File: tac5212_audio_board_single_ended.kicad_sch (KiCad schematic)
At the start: 94 parts, among them J1002 TAC5212, U1 Single Buffer - 74LVC1G125GV,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, U2 3.3v LDO - TLV74133PDBVR

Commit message: UPDATE
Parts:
- added G108: jumper, project_fp:jumper_slice, symbol proejct_lib:Jumper_2_Bridged
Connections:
- net Earth: now also E1.1 (A), E2.1 (A), G108.2 (B); no longer E1.2 (B), E2.2 (B)
- net GNDD: no longer T*C1.2, T*C2.2, T*C3.2, U2.2 (GND)
- net at board_outline1.49 (AGND): now also E1.2 (B); no longer E1.1 (A)
- net at board_outline1.50 (AGND): now also E2.2 (B); no longer E2.1 (A)
- new net: G108.1 (A), T*C1.2, T*C2.2, T*C3.2, U2.2 (GND)
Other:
- moved on the sheet: E1, E2
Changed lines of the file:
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@@
 	(wire
 		(pts
+			(xy 110.49 372.11) (xy 104.14 372.11)
+		)
+		(stroke
+			(width 0)
+			(type default)
+		)
+	)
+	(wire
+		(pts
 			(xy 218.44 168.91) (xy 222.25 168.91)
 		)
@@
 	(wire
 		(pts
-			(xy 90.17 367.03) (xy 90.17 365.76)
-		)
-		(stroke
-			(width 0)
-			(type default)
-		)
-	)
-	(wire
-		(pts
 			(xy 190.5 91.44) (xy 199.39 91.44)
 		)
@@
 	(wire
 		(pts
+			(xy 90.17 372.11) (xy 93.98 372.11)
+		)
+		(stroke
+			(width 0)
+			(type default)
+		)
+	)
+	(wire
+		(pts
 			(xy 49.53 294.64) (xy 66.04 294.64)
 		)
@@
 	(wire
 		(pts
+			(xy 90.17 372.11) (xy 90.17 365.76)
+		)
+		(stroke
+			(width 0)
+			(type default)
+		)
+	)
+	(wire
+		(pts
 			(xy 71.12 156.21) (xy 71.12 157.48)
 		)
@@
 	)
 	(symbol
+		(lib_id "proejct_lib:Earth")
+		(at 110.49 372.11 0)
+		(mirror y)
+		(unit 1)
+		(exclude_from_sim no)
+		(in_bom yes)
+		(on_board yes)
+		(dnp no)
+		(fields_autoplaced yes)
+		(property "Reference" "#PWR0108"
+			(at 110.49 378.46 0)
+			(effects
+				(font
+					(size 1 1)
+				)
+				(hide yes)
+			)
+		)
+		(property "Value" "Earth"
+			(at 110.49 375.92 0)
+			(effects
+				(font
+					(size 0.8 0.8)
+				)
+				(hide yes)
+			)
+		)
+		(property "Footprint" ""
+			(at 110.49 372.11 0)
+			(effects
+				(font
+					(size 0.8 0.8)
+				)
+				(hide yes)
+			)
+		)
+		(property "Datasheet" "~"
+			(at 110.49 372.11 0)
+			(effects
+				(font
+					(size 0.8 0.8)
+				)
+				(hide yes)
+			)
+		)
+		(property "Description" ""
+			(at 110.49 372.11 0)
+			(effects
+				(font
+					(size 1.27 1.27)
+				)
+				(hide yes)
+			)
+		)
+		(pin "1"
+		)
+		(instances
+			(project "tac5212_audio_board_single_ended"
+				(path "/8cee3af6-3893-45a9-89a4-21657973eeff"
+					(reference "#PWR0108")
+					(unit 1)
+				)
+			)
+		)
+	)
+	(symbol
 		(lib_name "Jumper_NO_Small-Device_1")
 		(lib_id "proejct_lib:Jumper_NO_Small-Device_1")
@@
 	(symbol
 		(lib_id "proejct_lib:Jumper_2_Bridged")
-		(at 125.73 287.02 0)
+		(at 125.73 287.02 180)
 		(unit 1)
 		(exclude_from_sim yes)
@@
 		(dnp yes)
 		(property "Reference" "E2"
-			(at 131.064 283.464 0)
+			(at 120.396 290.576 0)
 			(effects
 				(font
@@
 		)
 		(property "Value" "jumper"
-			(at 119.38 283.21 0)
+			(at 132.08 290.83 0)
 			(effects
 				(font
@@
 	)
 	(symbol
-		(lib_id "proejct_lib:GNDD")
-		(at 90.17 367.03 0)
-		(unit 1)
-		(exclude_from_sim no)
-		(in_bom yes)
-		(on_board yes)
-		(dnp no)
-		(fields_autoplaced yes)
-		(property "Reference" "#PWR013"
-			(at 90.17 373.38 0)
-			(effects
-				(font
-					(size 1 1)
-				)
-				(hide yes)
-			)
-		)
-		(property "Value" "GNDD"
-			(at 90.17 371.094 0)
-			(effects
-				(font
-					(size 0.8 0.8)
-				)
-			)
-		)
-		(property "Footprint" ""
-			(at 90.17 367.03 0)
-			(effects
-				(font
-					(size 0.8 0.8)
-				)
-				(hide yes)
-			)
-		)
-		(property "Datasheet" ""
-			(at 90.17 367.03 0)
-			(effects
-				(font
-					(size 0.8 0.8)
-				)
-				(hide yes)
-			)
-		)
-		(property "Description" ""
-			(at 90.17 367.03 0)
-			(effects
-				(font
-					(size 1.27 1.27)
-				)
-				(hide yes)
-			)
-		)
-		(pin "1"
-		)
-		(instances
-			(project "tac5212_audio_board_single_ended"
-				(path "/8cee3af6-3893-45a9-89a4-21657973eeff"
-					(reference "#PWR013")
-					(unit 1)
-				)
-			)
-		)
-	)
-	(symbol
 		(lib_id "proejct_lib:Jumper_NO_Small-Device")
 		(at 241.3 118.11 0)
@@
 	)
 	(symbol
+		(lib_id "proejct_lib:Jumper_2_Bridged")
+		(at 99.06 372.11 0)
+		(unit 1)
+		(exclude_from_sim yes)
+		(in_bom yes)
+		(on_board yes)
+		(dnp yes)
+		(property "Reference" "G108"
+			(at 104.394 371.094 0)
+			(effects
+				(font
+					(size 1.27 1.27)
+				)
+			)
+		)
+		(property "Value" "jumper"
+			(at 92.71 370.84 0)
+			(effects
+				(font
+					(size 1.27 1.27)
+				)
+				(hide yes)
+			)
+		)
+		(property "Footprint" "project_fp:jumper_slice"
+			(at 99.06 372.11 0)
+			(effects
+				(font
+					(size 1.27 1.27)
+				)
+				(hide yes)
+			)
+		)
+		(property "Datasheet" "~"
+			(at 99.06 372.11 0)
+			(effects
+				(font
+					(size 1.27 1.27)
+				)
+				(hide yes)
+			)
+		)
+		(property "Description" "Jumper, open"
+			(at 99.06 372.11 0)
+			(effects
+				(font
+					(size 1.27 1.27)
+				)
+				(hide yes)
+			)
+		)
+		(property "Label" "G"
+			(at 99.06 372.11 0)
+			(effects
+				(font
+					(size 1.27 1.27)
+				)
+				(hide yes)
+			)
+		)
+		(property "Package / Case" "DNP"
+			(at 99.06 372.11 0)
+			(effects
+				(font
+					(size 1.27 1.27)
+				)
+				(hide yes)
+			)
+		)
+		(property "TAC5212EVM" "n/a"
+			(at 99.06 372.11 0)
+			(effects
+				(font
+					(size 1.27 1.27)
+				)
+				(hide yes)
+			)
+		)
+		(pin "1"
+		)
+		(pin "2"
+		)
+		(instances
+			(project "tac5212_audio_board_single_ended"
+				(path "/8cee3af6-3893-45a9-89a4-21657973eeff"
+					(reference "G108")
+					(unit 1)
+				)
+			)
+		)
+	)
+	(symbol
 		(lib_id "proejct_lib:GNDD")
 		(at 144.78 162.56 0)
@@
 	(symbol
 		(lib_id "proejct_lib:Jumper_2_Bridged")
-		(at 125.73 281.94 0)
+		(at 125.73 281.94 180)
 		(unit 1)
 		(exclude_from_sim yes)
@@
 		(dnp yes)
 		(property "Reference" "E1"
-			(at 131.064 280.924 0)
+			(at 120.396 282.956 0)
 			(effects
 				(font
@@
 		)
 		(property "Value" "jumper"
-			(at 119.38 280.67 0)
+			(at 132.08 283.21 0)
 			(effects
 				(font

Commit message: update
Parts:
- board_outline1: now not fitted
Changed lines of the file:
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@@
 		(in_bom yes)
 		(on_board yes)
-		(dnp no)
+		(dnp yes)
 		(property "Reference" "board_outline1"
 			(at 91.44 217.17 0)

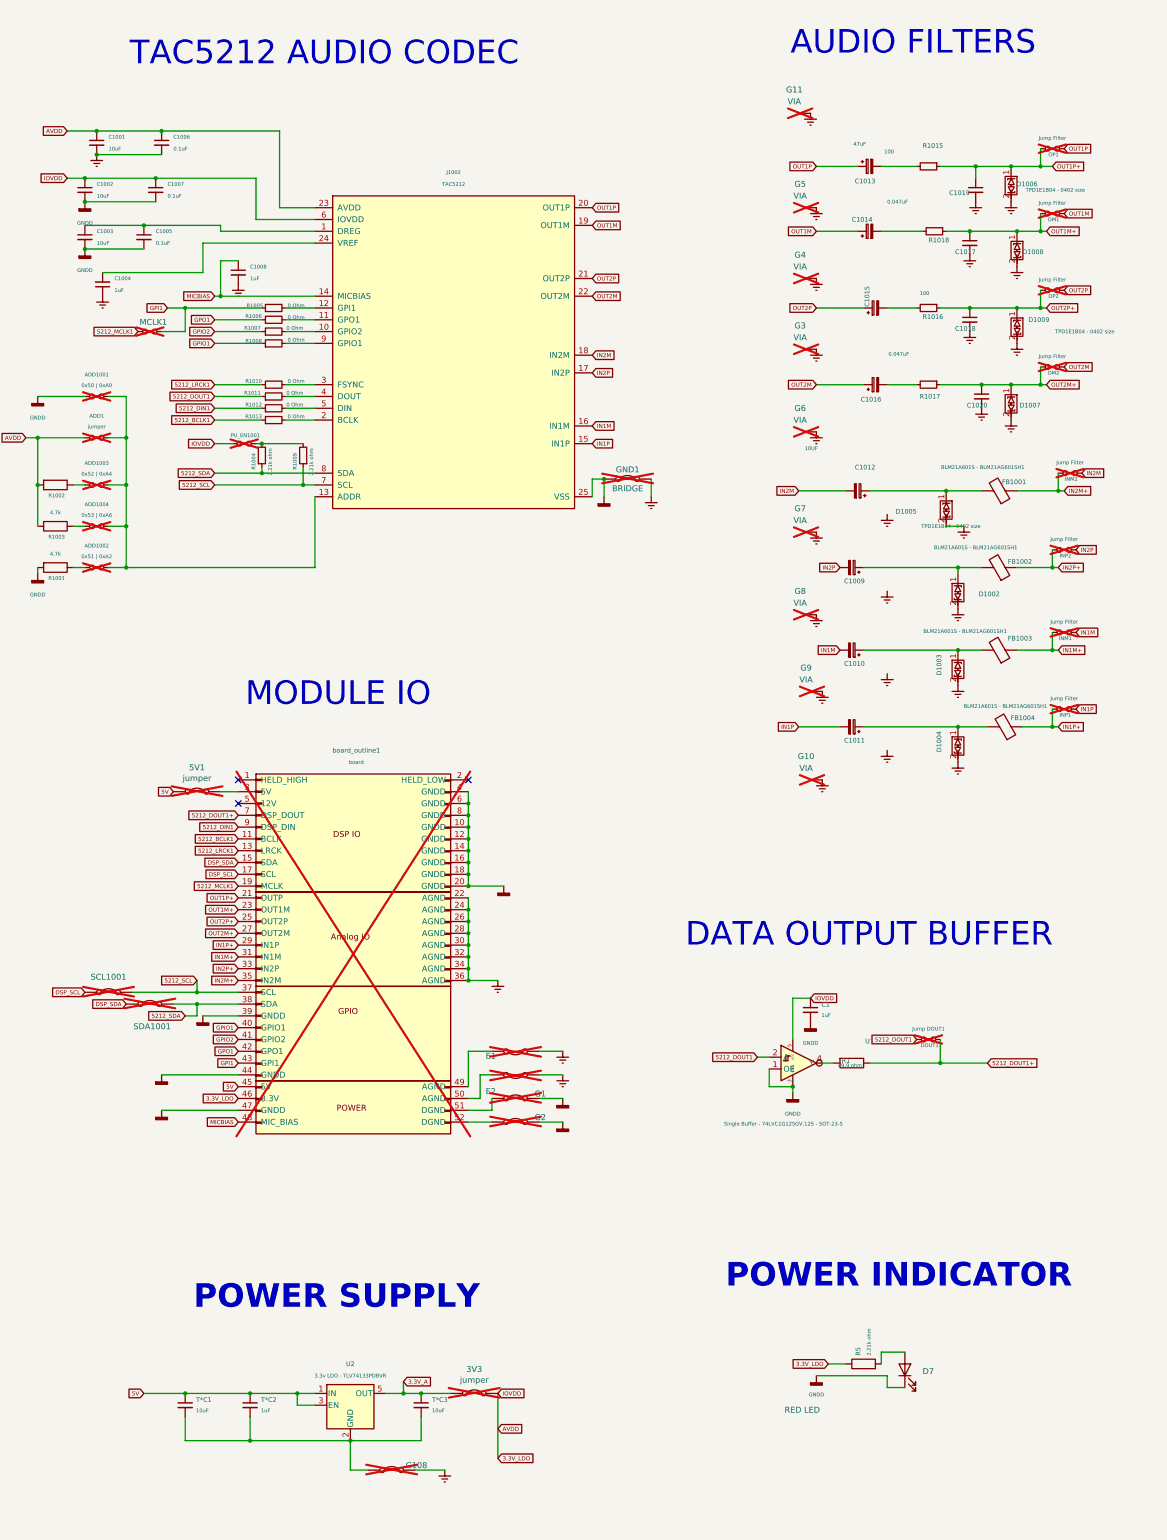
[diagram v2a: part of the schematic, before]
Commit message: added enable (held-high)
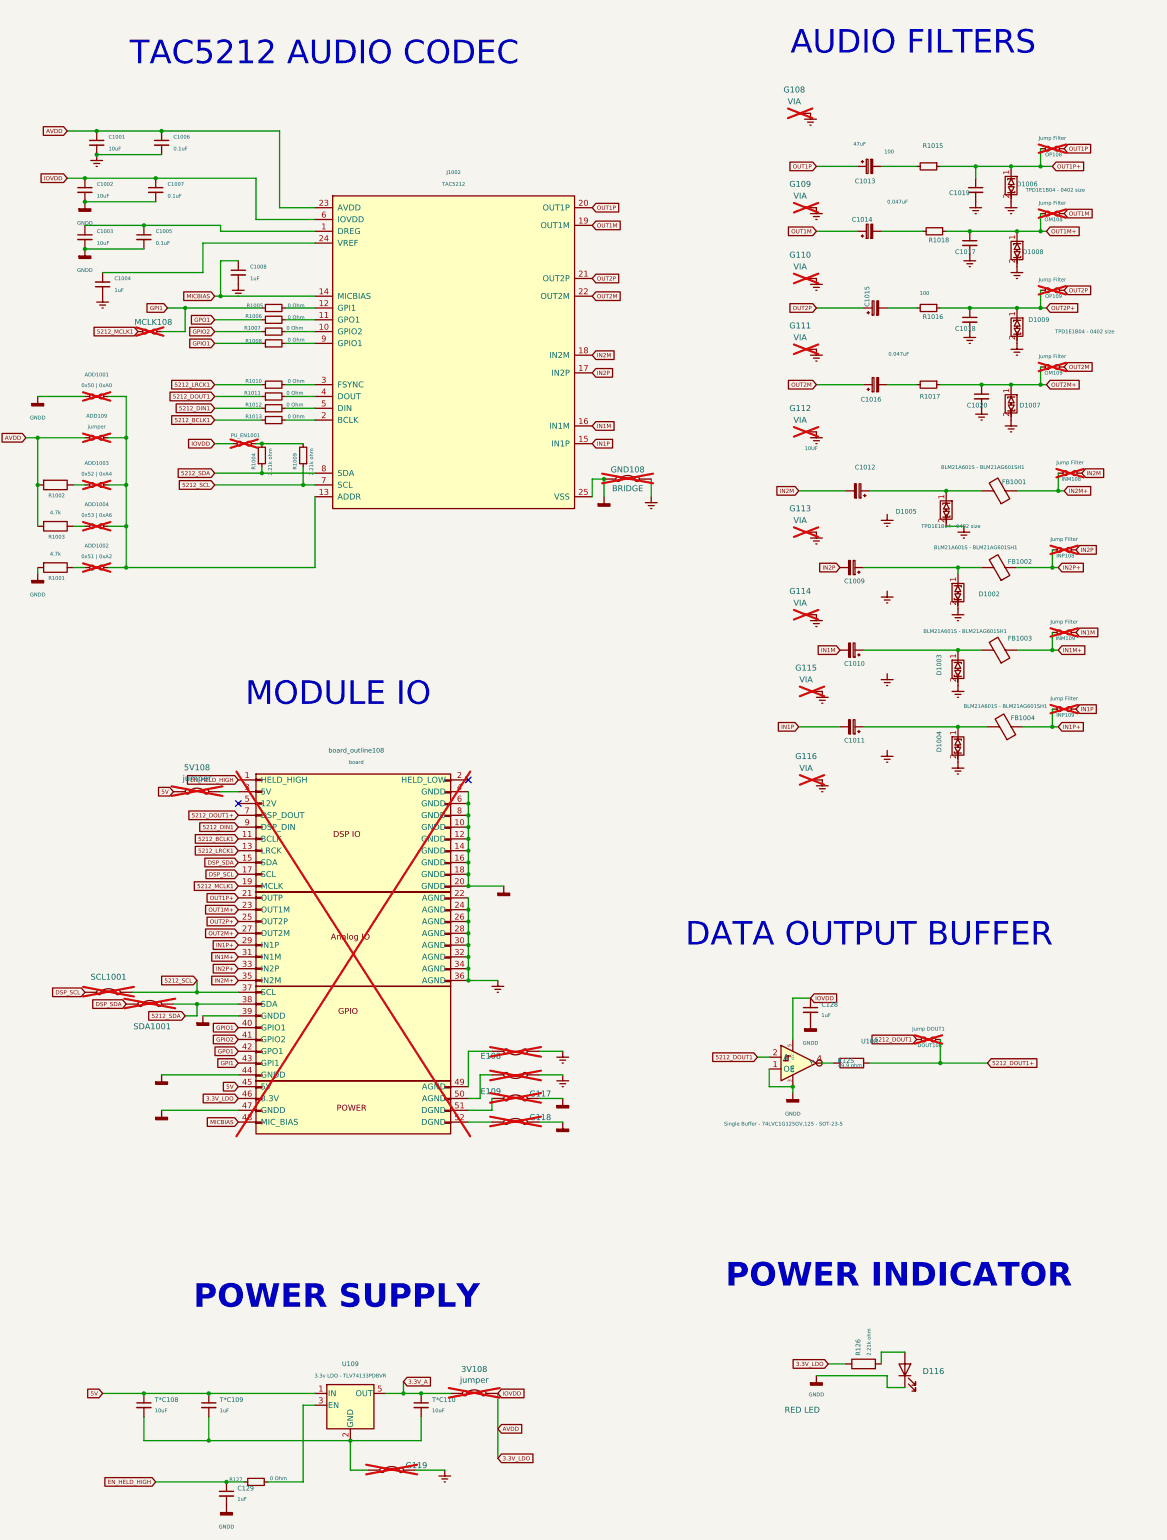
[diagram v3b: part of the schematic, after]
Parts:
- added C129: 1uF, Capacitor_SMD:C_0603_1608Metric_Pad1.08x0.95mm_HandSolder, symbol proejct_lib:C_Small
- added R127: 0 Ohm, Resistor_SMD:R_0402_1005Metric_Pad0.72x0.64mm_HandSolder, symbol proejct_lib:R_Small
- renumbered 3V3 to 3V108, 5V1 to 5V108, ADD1 to ADD109, C1 to C128, D7 to D116, DOUT1 to DOUT108, E1 to E108, E2 to E109, G11 to G108, G5 to G109, G4 to G110, G3 to G111, G6 to G112, G7 to G113, G8 to G114, G9 to G115, G10 to G116, G1 to G117, G2 to G118, G108 to G119, GND1 to GND108, INM2 to INM108, INM1 to INM109, INP2 to INP108, INP1 to INP109, MCLK1 to MCLK108, OM1 to OM108, OM2 to OM109, OP1 to OP108, OP2 to OP109, R1 to R125, R5 to R126, T*C1 to T*C108, T*C2 to T*C109, T*C3 to T*C110, U1 to U108, U2 to U109, board_outline1 to board_outline108
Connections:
- net 5V: no longer U109.3 (EN)
- net GNDD: now also C129.2
- net EN_HELD_HIGH: now reaches board_outline108.1 (HELD_HIGH)
- net EN_HELD_HIGH: now also C129.1, R127.1
- new net: R127.2, U109.3 (EN)
- no-connect marks 3 -> 2
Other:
- moved on the sheet: T*C108, T*C109

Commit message: update
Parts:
- R1004, R1009: TAC5212EVM RC0402FR-07100KL -> RC0402FR-072K21L
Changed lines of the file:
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@@
 			)
 		)
-		(property "TAC5212EVM" "RC0402FR-07100KL"
+		(property "TAC5212EVM" "RC0402FR-072K21L"
 			(at 71.12 153.67 0)
 			(effects
@@
 			)
 		)
-		(property "TAC5212EVM" "RC0402FR-07100KL"
+		(property "TAC5212EVM" "RC0402FR-072K21L"
 			(at 80.01 153.67 0)
 			(effects

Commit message: update
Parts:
- removed ADD109: jumper, project_fp:SolderJumper-2_Open_Pad0.5x1.0mm_ADDR, symbol proejct_lib:Jumper_NO_Small-Device
- J1002: footprint project_fp:TAC5212IRGER-24-1EP_4x4mm -> project_fp:VQFN-24-1EP_4x4mm_P0.5mm_EP2.45x2.45mm_ThermalVias
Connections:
- net GNDD: now also J1002.A1 (VSS), J1002.A2 (VSS), J1002.A3 (VSS), J1002.A4 (VSS)
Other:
- moved on the sheet: ADD1001, ADD1003, ADD1004, GND108, R1002, R1003

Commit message: update
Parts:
- renumbered INM109 to INM1, INM108 to INM2, INP109 to INP1, INP108 to INP2, OM108 to OM1, OM109 to OM2, OP108 to OP1, OP109 to OP2
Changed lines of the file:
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@@
 		(on_board yes)
 		(dnp yes)
-		(property "Reference" "INM109"
+		(property "Reference" "INM1"
 			(at 244.094 193.04 0)
 			(effects
@@
 			(project "tac5212_audio_board_single_ended"
 				(path "/8cee3af6-3893-45a9-89a4-21657973eeff"
-					(reference "INM109")
+					(reference "INM1")
 					(unit 1)
 				)
@@
 		(on_board yes)
 		(dnp yes)
-		(property "Reference" "OP108"
+		(property "Reference" "OP1"
 			(at 241.554 88.9 0)
 			(effects
@@
 			(project "tac5212_audio_board_single_ended"
 				(path "/8cee3af6-3893-45a9-89a4-21657973eeff"
-					(reference "OP108")
+					(reference "OP1")
 					(unit 1)
 				)
@@
 		(on_board yes)
 		(dnp yes)
-		(property "Reference" "OM109"
+		(property "Reference" "OM2"
 			(at 241.554 135.89 0)
 			(effects
@@
 			(project "tac5212_audio_board_single_ended"
 				(path "/8cee3af6-3893-45a9-89a4-21657973eeff"
-					(reference "OM109")
+					(reference "OM2")
 					(unit 1)
 				)
@@
 		(on_board yes)
 		(dnp yes)
-		(property "Reference" "OM108"
+		(property "Reference" "OM1"
 			(at 241.554 102.87 0)
 			(effects
@@
 			(project "tac5212_audio_board_single_ended"
 				(path "/8cee3af6-3893-45a9-89a4-21657973eeff"
-					(reference "OM108")
+					(reference "OM1")
 					(unit 1)
 				)
@@
 		(on_board yes)
 		(dnp yes)
-		(property "Reference" "INP109"
+		(property "Reference" "INP1"
 			(at 244.094 209.55 0)
 			(effects
@@
 			(project "tac5212_audio_board_single_ended"
 				(path "/8cee3af6-3893-45a9-89a4-21657973eeff"
-					(reference "INP109")
+					(reference "INP1")
 					(unit 1)
 				)
@@
 		(on_board yes)
 		(dnp yes)
-		(property "Reference" "INM108"
+		(property "Reference" "INM2"
 			(at 245.364 158.75 0)
 			(effects
@@
 			(project "tac5212_audio_board_single_ended"
 				(path "/8cee3af6-3893-45a9-89a4-21657973eeff"
-					(reference "INM108")
+					(reference "INM2")
 					(unit 1)
 				)
@@
 		(on_board yes)
 		(dnp yes)
-		(property "Reference" "INP108"
+		(property "Reference" "INP2"
 			(at 244.094 175.26 0)
 			(effects
@@
 			(project "tac5212_audio_board_single_ended"
 				(path "/8cee3af6-3893-45a9-89a4-21657973eeff"
-					(reference "INP108")
+					(reference "INP2")
 					(unit 1)
 				)
@@
 		(on_board yes)
 		(dnp yes)
-		(property "Reference" "OP109"
+		(property "Reference" "OP2"
 			(at 241.554 119.38 0)
 			(effects
@@
 			(project "tac5212_audio_board_single_ended"
 				(path "/8cee3af6-3893-45a9-89a4-21657973eeff"
-					(reference "OP109")
+					(reference "OP2")
 					(unit 1)
 				)

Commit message: update
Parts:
- added TAC108-Q1: TAC5212-Q1, Package_DFN_QFN:Texas_RHB0032E_VQFN-32-1EP_5x5mm_P0.5mm_EP3.45x3.45mm_ThermalVias, symbol proejct_lib:TAC5212-Q1-WQFN-32
- J1002: now not fitted
- R1011: value 0 Ohm -> 49.9 ohm; TAC5212EVM ERJ-2GE0R00X -> (none)
- R126: REPLACE FOR NEXT BUILD (none) -> RC0402FR-072K21L
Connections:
- net 3.3V_LDO: now also TAC108-Q1.31 (AVDD), TAC108-Q1.7 (IOVDD)
- net 5212_SCL: now also TAC108-Q1.9 (SCL)
- net 5212_SDA: now also TAC108-Q1.10 (SDA)
- net GNDD: now also TAC108-Q1. (VSS), TAC108-Q1.1 (VSS), TAC108-Q1.26 (AVSS), TAC108-Q1.33 (VSS), TAC108-Q1.8 (IOVSS); no longer board_outline108.4 (GNDD)
- net IN1M: now also TAC108-Q1.19 (IN1M)
- net IN1P: now also TAC108-Q1.18 (IN1P)
- net IN2M: now also TAC108-Q1.21 (IN2M)
- net IN2P: now also TAC108-Q1.20 (IN2P)
- net MICBIAS: now also TAC108-Q1.17 (MICBIAS)
- net OUT1M: now also TAC108-Q1.27 (OUT1M)
- net OUT1P: now also TAC108-Q1.28 (OUT1P)
- net OUT2M: now also TAC108-Q1.30 (OUT2M)
- net OUT2P: now also TAC108-Q1.29 (OUT2P)
- net at J1002.11 (GPO1), R1006.2: now also TAC108-Q1.11 (GPO1)
- net at C1004.2, J1002.24 (VREF): now also TAC108-Q1.32 (VREF)
- net at C1003.1, C1005.1, J1002.1 (DREG): now also TAC108-Q1.2 (DREG)
- net at J1002.10 (GPIO2), R1007.2: now also TAC108-Q1.24 (GPIO2)
- net at J1002.5 (DIN), R1012.2: now also TAC108-Q1.6 (DIN)
- net at J1002.12 (GPI1), R1005.2: now also TAC108-Q1.25 (GPI1)
- net at ADD1001.2, ADD1002.2, ADD1003.2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: now also TAC108-Q1.22 (ADDR)
- net at J1002.9 (GPIO1), R1008.2: now also TAC108-Q1.23 (GPIO1)
- net at J1002.2 (BCLK), R1013.2: now also TAC108-Q1.3 (BCLK)
- net at J1002.4 (DOUT), R1011.2: now also TAC108-Q1.5 (DOUT)
- net at J1002.3 (FSYNC), R1010.2: now also TAC108-Q1.4 (FSYNC)
- no-connect marks 2 -> 8
